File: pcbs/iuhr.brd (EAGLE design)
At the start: 38.4 x 23 mm, 75 parts, among them IC1 TPS77033, Q1 20.000MHz

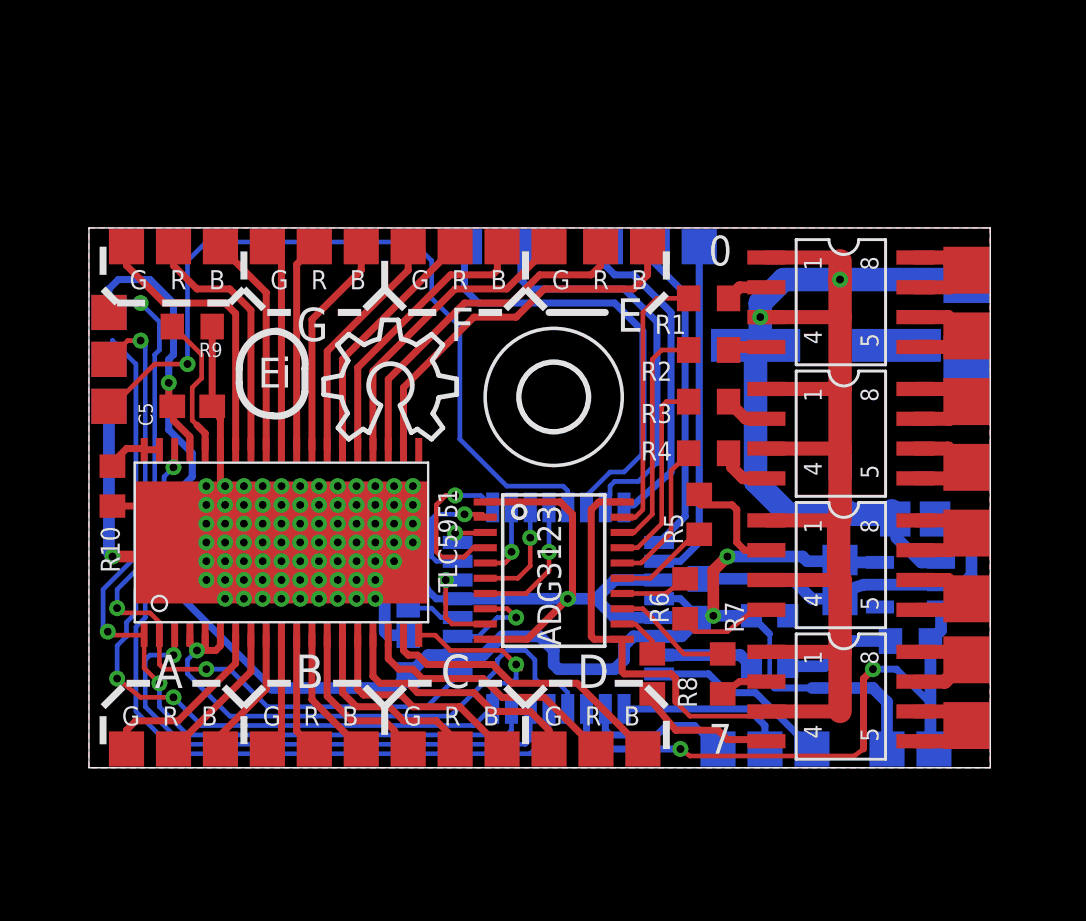
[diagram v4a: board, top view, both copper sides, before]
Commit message: Further improve silkscreen.
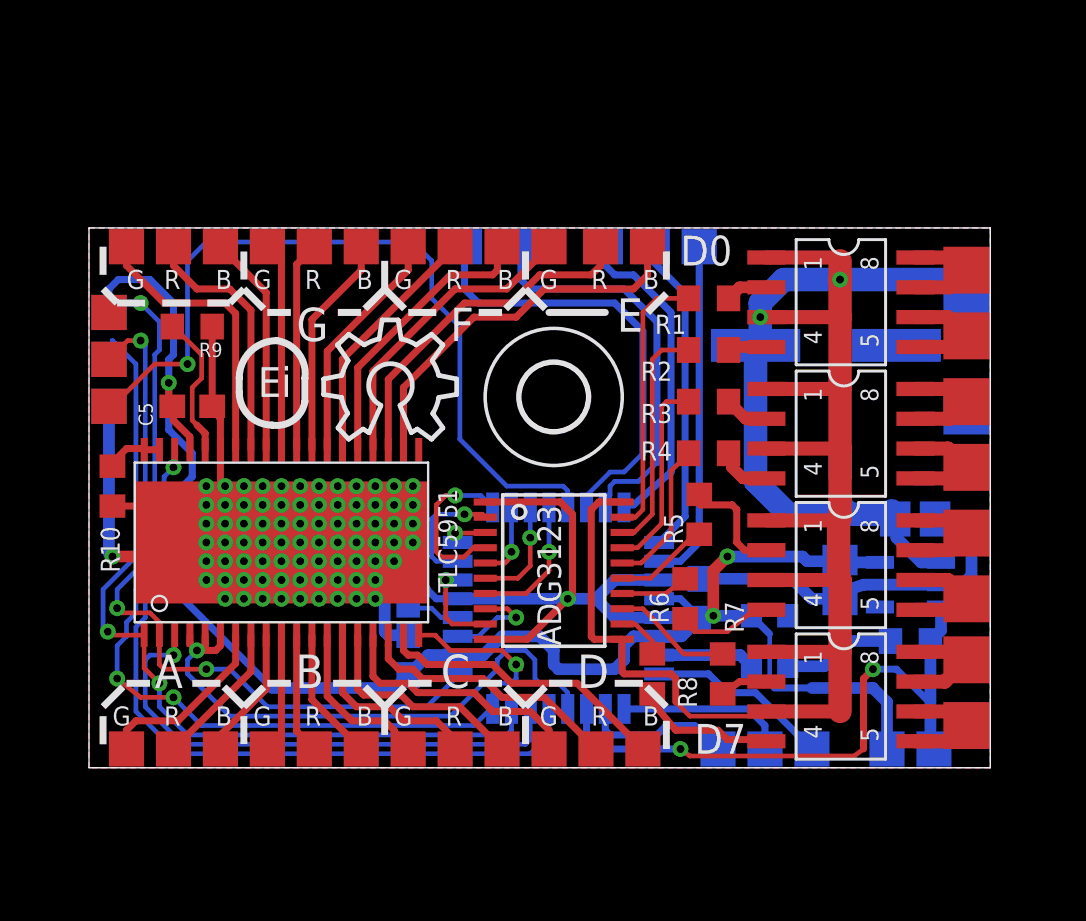
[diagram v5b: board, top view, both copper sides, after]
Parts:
- moved GND_IN 2.20 mm to (37.4, 15.2)
- moved 12V_IN 0.80 mm to (37.4, 20.0)
- renumbered IC1 to TPS70933
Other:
- board text added: "D0"
- board text added: "D7"
- board text added: "R"
- board text added: "licensed under CERN OHL v1.2"
- board text added: "powered by xpcc"
- board text removed: "0"
- board text removed: "7"
- board text removed: "G R B"
- board text removed: "Licence: CERN OHL v1.2"

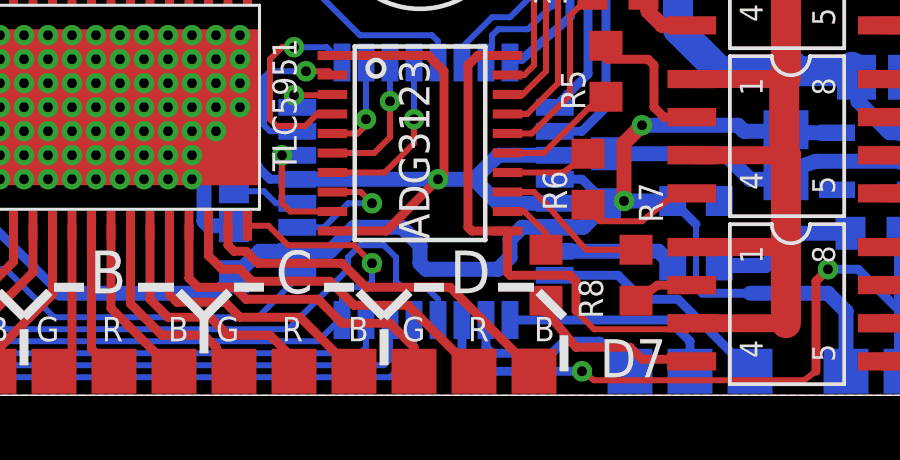
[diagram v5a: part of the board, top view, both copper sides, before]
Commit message: VCC: 3.3V -> 5V; add cap for adg3123
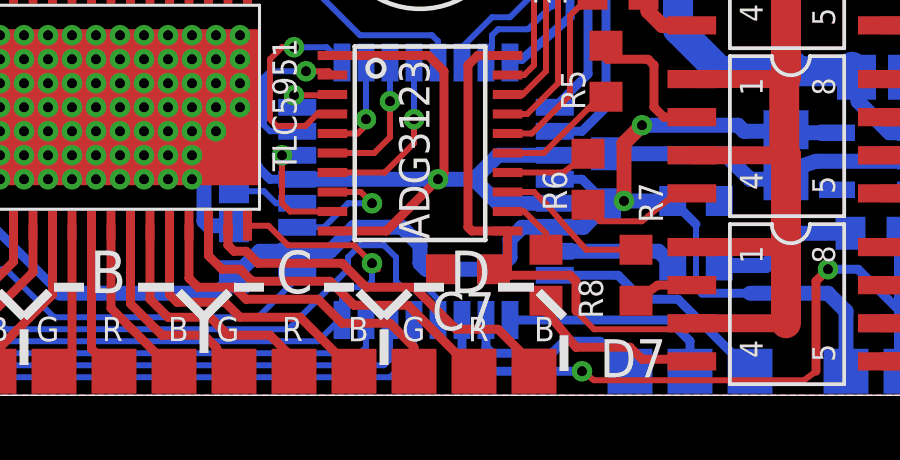
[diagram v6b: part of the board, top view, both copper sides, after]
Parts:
- added C7: 100nF, resistor:C0603
- TPS70933: value TPS77033 -> TPS77050
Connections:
- net +12V: now also C7.1
- net GND: now also C7.2
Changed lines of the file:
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@@
 <grid distance="0.2" unitdist="mm" unit="mm" style="dots" multiple="1" display="yes" altdistance="0.15875" altunitdist="mm" altunit="mm"/>
 <layers>
-<layer number="1" name="Top" color="4" fill="1" visible="no" active="yes"/>
+<layer number="1" name="Top" color="4" fill="1" visible="yes" active="yes"/>
 <layer number="2" name="Route2" color="1" fill="3" visible="no" active="no"/>
 <layer number="3" name="Route3" color="4" fill="3" visible="no" active="no"/>
@@
 <layer number="19" name="Unrouted" color="6" fill="1" visible="yes" active="yes"/>
 <layer number="20" name="Dimension" color="15" fill="1" visible="yes" active="yes"/>
-<layer number="21" name="tPlace" color="7" fill="1" visible="no" active="yes"/>
+<layer number="21" name="tPlace" color="7" fill="1" visible="yes" active="yes"/>
 <layer number="22" name="bPlace" color="7" fill="1" visible="yes" active="yes"/>
-<layer number="23" name="tOrigins" color="15" fill="1" visible="no" active="yes"/>
+<layer number="23" name="tOrigins" color="15" fill="1" visible="yes" active="yes"/>
 <layer number="24" name="bOrigins" color="15" fill="1" visible="yes" active="yes"/>
-<layer number="25" name="tNames" color="7" fill="1" visible="no" active="yes"/>
+<layer number="25" name="tNames" color="7" fill="1" visible="yes" active="yes"/>
 <layer number="26" name="bNames" color="7" fill="1" visible="yes" active="yes"/>
 <layer number="27" name="tValues" color="7" fill="1" visible="no" active="yes"/>
@@
 <layer number="37" name="tTest" color="7" fill="1" visible="no" active="yes"/>
 <layer number="38" name="bTest" color="7" fill="1" visible="no" active="yes"/>
-<layer number="39" name="tKeepout" color="4" fill="11" visible="no" active="yes"/>
+<layer number="39" name="tKeepout" color="4" fill="11" visible="yes" active="yes"/>
 <layer number="40" name="bKeepout" color="1" fill="11" visible="yes" active="yes"/>
 <layer number="41" name="tRestrict" color="4" fill="10" visible="no" active="yes"/>
@@
 <layer number="49" name="Reference" color="7" fill="1" visible="no" active="yes"/>
 <layer number="50" name="dxf" color="7" fill="1" visible="no" active="no"/>
-<layer number="51" name="tDocu" color="7" fill="1" visible="no" active="yes"/>
+<layer number="51" name="tDocu" color="7" fill="1" visible="yes" active="yes"/>
 <layer number="52" name="bDocu" color="7" fill="1" visible="yes" active="yes"/>
 <layer number="53" name="tGND_GNDA" color="7" fill="9" visible="no" active="no"/>
@@
 <attribute name="VALUE" x="3.032" y="11.111" size="1.27" layer="27" rot="R90"/>
 </element>
-<element name="TPS70933" library="texas" package="SOT23-DBV" value="TPS77033" x="35" y="7.8" smashed="yes" rot="MR270">
-<attribute name="OC_NEWARK" value="77C1187" x="61.67" y="-41.73" size="1.778" layer="28" rot="MR270" display="off"/>
-<attribute name="MPN" value="TPS77033DBVT" x="61.67" y="-41.73" size="1.778" layer="28" rot="MR270" display="off"/>
-<attribute name="MF" value="TEXAS INSTRUMENTS" x="61.67" y="-41.73" size="1.778" layer="28" rot="MR270" display="off"/>
-<attribute name="OC_FARNELL" value="8461570" x="61.67" y="-41.73" size="1.778" layer="28" rot="MR270" display="off"/>
+<element name="TPS70933" library="texas" package="SOT23-DBV" value="TPS77050" x="35" y="7.8" smashed="yes" rot="MR270">
+<attribute name="OC_NEWARK" value="77C1189" x="61.67" y="-41.73" size="1.778" layer="28" rot="MR270" display="off"/>
+<attribute name="MPN" value="TPS77050DBVT" x="61.67" y="-41.73" size="1.778" layer="28" rot="MR270" display="off"/>
+<attribute name="MF" value="TEXAS INSTRUMENT CONNECTORS" x="61.67" y="-41.73" size="1.778" layer="28" rot="MR270" display="off"/>
+<attribute name="OC_FARNELL" value="1412883" x="61.67" y="-41.73" size="1.778" layer="28" rot="MR270" display="off"/>
 <attribute name="NAME" x="37.895" y="9.705" size="0.8128" layer="26" rot="MR270"/>
 <attribute name="VALUE" x="38.429" y="9.705" size="1.27" layer="28" rot="MR270"/>
@@
 <attribute name="VALUE" x="31.562" y="-0.089" size="0.0254" layer="28" rot="MR0"/>
 </element>
+<element name="C7" library="resistor" package="C0603" value="100nF" x="21.4" y="4.2" rot="R180"/>
 </elements>
 <signals>
@@
 <via x="11.4" y="7.2" extent="1-16" drill="0.3302"/>
 <via x="12.2" y="7.2" extent="1-16" drill="0.3302"/>
+<contactref element="C7" pad="2"/>
 </signal>
 <signal name="VCC">
@@
 <contactref element="DB" pad="TP"/>
 <contactref element="TLC5951" pad="18"/>
-<wire x1="18" y1="3.6" x2="20.8" y2="3.6" width="0.3" layer="1"/>
-<wire x1="20.8" y1="3.6" x2="23.6" y2="0.8" width="0.3" layer="1"/>
 <wire x1="14.4" y1="4.4" x2="17.2" y2="4.4" width="0.3" layer="1"/>
 <wire x1="17.2" y1="4.4" x2="18" y2="3.6" width="0.3" layer="1"/>
@@
 <wire x1="13.6" y1="4.8" x2="13.4" y2="5" width="0.3" layer="1"/>
 <wire x1="13.4" y1="5" x2="13.4" y2="5.65" width="0.3" layer="1"/>
+<wire x1="23.6" y1="0.8" x2="23.6" y2="1" width="0.3" layer="1"/>
+<wire x1="23.6" y1="1" x2="22.4" y2="2.2" width="0.3" layer="1"/>
+<wire x1="22.4" y1="2.2" x2="21" y2="2.2" width="0.3" layer="1"/>
+<wire x1="21" y1="2.2" x2="19.6" y2="3.6" width="0.3" layer="1"/>
+<wire x1="19.6" y1="3.6" x2="18" y2="3.6" width="0.3" layer="1"/>
 </signal>
 <signal name="N$16">
@@
 <wire x1="32" y1="11.15" x2="32.2" y2="11" width="1" layer="16"/>
 <wire x1="32.2" y1="11" x2="32.4" y2="10.8" width="1" layer="16"/>
+<contactref element="C7" pad="1"/>
+<wire x1="22.7178" y1="4.0822" x2="22.5678" y2="4.0822" width="0.3" layer="1"/>
+<wire x1="22.5678" y1="4.0822" x2="22.25" y2="4.2" width="0.3" layer="1"/>
 </signal>
 <signal name="N$29">

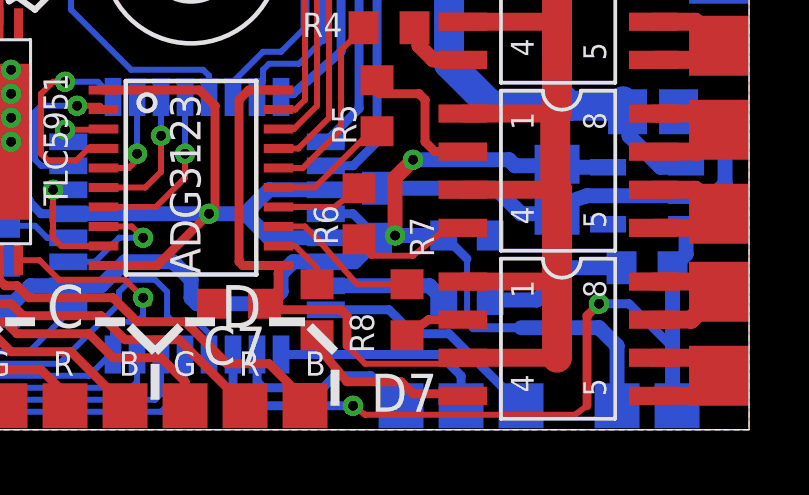
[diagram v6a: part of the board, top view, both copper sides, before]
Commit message: Power On: add cap and series resistor for button.
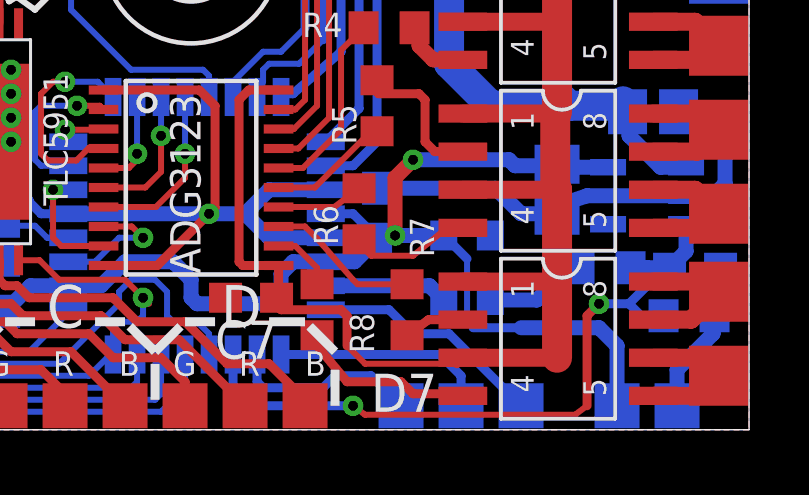
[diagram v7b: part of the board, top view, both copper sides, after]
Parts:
- added C8: tbd, resistor:C0603
- added R12: 100, resistor:R0603
- moved R11 1.40 mm to (33.6, 5.40)
- moved C7 0.45 mm to (21.8, 4.40)
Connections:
- new net N$59: ONBTN.TP, R12.2
- net GND: now also C8.2
- net ON: now also C8.1, R12.1; no longer ONBTN.TP
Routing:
- net ON: track 28.4 -> 23.8 mm
- net N$59: track 0.00 -> 3.52 mm
- net GND: track 93.2 -> 91.8 mm
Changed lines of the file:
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@@
 <attribute name="VALUE" x="38.429" y="9.705" size="1.27" layer="28" rot="MR270"/>
 </element>
-<element name="R11" library="resistor" package="R0603" value="10k" x="35" y="5.4" smashed="yes" rot="MR180">
-<attribute name="NAME" x="31.511" y="5.911" size="0.8128" layer="26" rot="MR180"/>
-<attribute name="VALUE" x="34.111" y="7.432" size="1.27" layer="28" rot="MR180"/>
+<element name="R11" library="resistor" package="R0603" value="10k" x="33.6" y="5.4" smashed="yes" rot="MR180">
+<attribute name="NAME" x="30.111" y="5.911" size="0.8128" layer="26" rot="MR180"/>
+<attribute name="VALUE" x="32.711" y="7.432" size="1.27" layer="28" rot="MR180"/>
 </element>
 <element name="C4" library="resistor" package="C0805" value="1uF" x="35.2" y="10.6" smashed="yes" rot="MR180">
@@
 <attribute name="VALUE" x="31.562" y="-0.089" size="0.0254" layer="28" rot="MR0"/>
 </element>
-<element name="C7" library="resistor" package="C0603" value="100nF" x="21.4" y="4.2" rot="R180"/>
+<element name="C7" library="resistor" package="C0603" value="100nF" x="21.8" y="4.4" rot="R180"/>
+<element name="C8" library="resistor" package="C0603" value="tbd" x="36.6" y="5.4" rot="MR180"/>
+<element name="R12" library="resistor" package="R0603" value="100" x="36.4" y="3.8" rot="MR180"/>
 </elements>
 <signals>
@@
 <wire x1="32" y1="5" x2="32" y2="5.6" width="0.5" layer="16"/>
 <wire x1="32" y1="5.6" x2="32" y2="7.15" width="0.5" layer="16"/>
-<wire x1="34.15" y1="5.4" x2="32.2" y2="5.4" width="0.5" layer="16"/>
+<wire x1="32.75" y1="5.4" x2="32.2" y2="5.4" width="0.5" layer="16"/>
 <wire x1="32.2" y1="5.4" x2="32" y2="5.6" width="0.5" layer="16"/>
 <wire x1="16.8822" y1="11.325" x2="20.075" y2="11.325" width="0.3" layer="1"/>
@@
 <via x="12.2" y="7.2" extent="1-16" drill="0.3302"/>
 <contactref element="C7" pad="2"/>
+<contactref element="C8" pad="2"/>
 </signal>
 <signal name="VCC">
@@
 <wire x1="32.2" y1="11" x2="32.4" y2="10.8" width="1" layer="16"/>
 <contactref element="C7" pad="1"/>
-<wire x1="22.7178" y1="4.0822" x2="22.5678" y2="4.0822" width="0.3" layer="1"/>
-<wire x1="22.5678" y1="4.0822" x2="22.25" y2="4.2" width="0.3" layer="1"/>
+<wire x1="22.65" y1="4.4" x2="22.65" y2="4.15" width="0.3" layer="1"/>
+<wire x1="22.65" y1="4.15" x2="22.7178" y2="4.0822" width="0.3" layer="1"/>
 </signal>
 <signal name="N$29">
@@
 <contactref element="R11" pad="2"/>
 <contactref element="ATMEGA88PA" pad="11"/>
-<contactref element="ONBTN" pad="TP"/>
-<wire x1="36.3" y1="6.85" x2="36.3" y2="5.85" width="0.5" layer="16"/>
-<wire x1="36.3" y1="5.85" x2="35.85" y2="5.4" width="0.5" layer="16"/>
-<wire x1="35.85" y1="5.4" x2="35.85" y2="0.85" width="0.5" layer="16"/>
-<wire x1="35.85" y1="0.85" x2="36" y2="0.8" width="0.5" layer="16"/>
-<wire x1="36" y1="0.8" x2="35.8" y2="2.8" width="0.3" layer="16"/>
-<wire x1="35.8" y1="2.8" x2="34.4" y2="4.2" width="0.3" layer="16"/>
 <wire x1="34.4" y1="4.2" x2="33.4" y2="4.2" width="0.3" layer="16"/>
 <via x="33.4" y="4.2" extent="1-16" drill="0.3302"/>
@@
 <wire x1="21.6" y1="0.8" x2="21.2" y2="1.2" width="0.3" layer="16"/>
 <wire x1="21.2" y1="1.2" x2="21.2" y2="2.5074" width="0.3" layer="16"/>
+<contactref element="C8" pad="1"/>
+<contactref element="R12" pad="1"/>
+<wire x1="36.3" y1="6.85" x2="36.3" y2="5.95" width="0.5" layer="16"/>
+<wire x1="36.3" y1="5.95" x2="35.75" y2="5.4" width="0.5" layer="16"/>
+<wire x1="35.75" y1="5.4" x2="35" y2="5.4" width="0.5" layer="16"/>
+<wire x1="35" y1="5.4" x2="34.45" y2="5.4" width="0.5" layer="16"/>
+<wire x1="35.55" y1="3.8" x2="34.8" y2="3.8" width="0.3" layer="16"/>
+<wire x1="34.8" y1="3.8" x2="34.4" y2="4.2" width="0.3" layer="16"/>
+<wire x1="34.4" y1="4.2" x2="35" y2="4.8" width="0.3" layer="16"/>
+<wire x1="35" y1="4.8" x2="35" y2="5.4" width="0.3" layer="16"/>
 </signal>
 <signal name="N$7">
@@
 <wire x1="28.4" y1="3.2" x2="30.8" y2="0.8" width="0.3" layer="16"/>
 </signal>
+<signal name="N$59">
+<contactref element="ONBTN" pad="TP"/>
+<contactref element="R12" pad="2"/>
+<wire x1="36" y1="0.8" x2="36" y2="2" width="0.5" layer="16"/>
+<wire x1="36" y1="2" x2="37.2" y2="3.2" width="0.5" layer="16"/>
+<wire x1="37.2" y1="3.2" x2="37.2" y2="3.75" width="0.5" layer="16"/>
+<wire x1="37.2" y1="3.75" x2="37.25" y2="3.8" width="0.5" layer="16"/>
+</signal>
 </signals>
